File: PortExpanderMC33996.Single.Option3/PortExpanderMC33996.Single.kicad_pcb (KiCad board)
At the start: 2 copper layers, 8 parts, among them J1 DEBUG_CON_01X09, J2 VIKING_CON_01X09, J3 VIKING_CON_01X09, J4 SATA_CON_14P, U1 MC33996EKR2

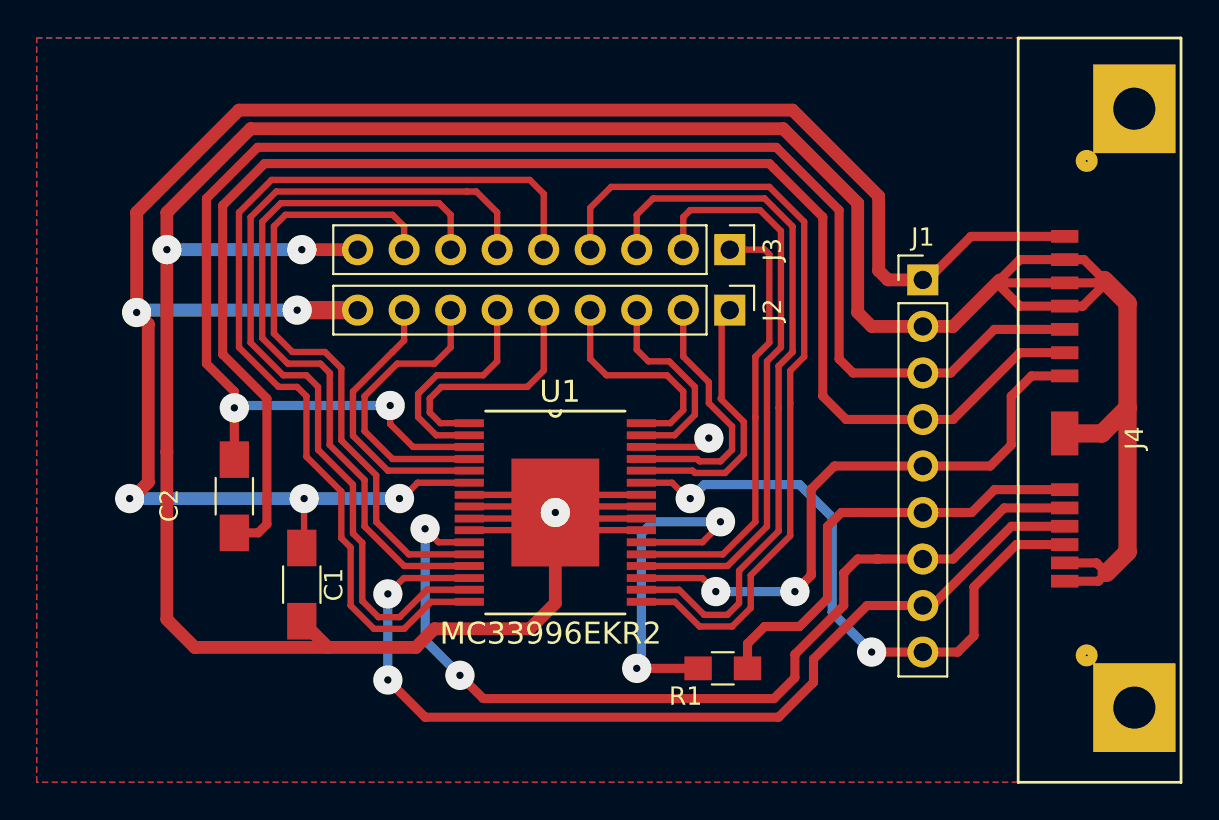
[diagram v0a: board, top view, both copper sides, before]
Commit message: Revision de PCbs + generacion de nuevos archivos Gerber
  - Se corrigen pads de pin headers
  - Se revisan
  - MainBoard option 2
  - PortExpander MC33996.Option3
  - GpibPortExpanderPCA6408A.Option3
  - Se generan Gerber + Vistas 3D
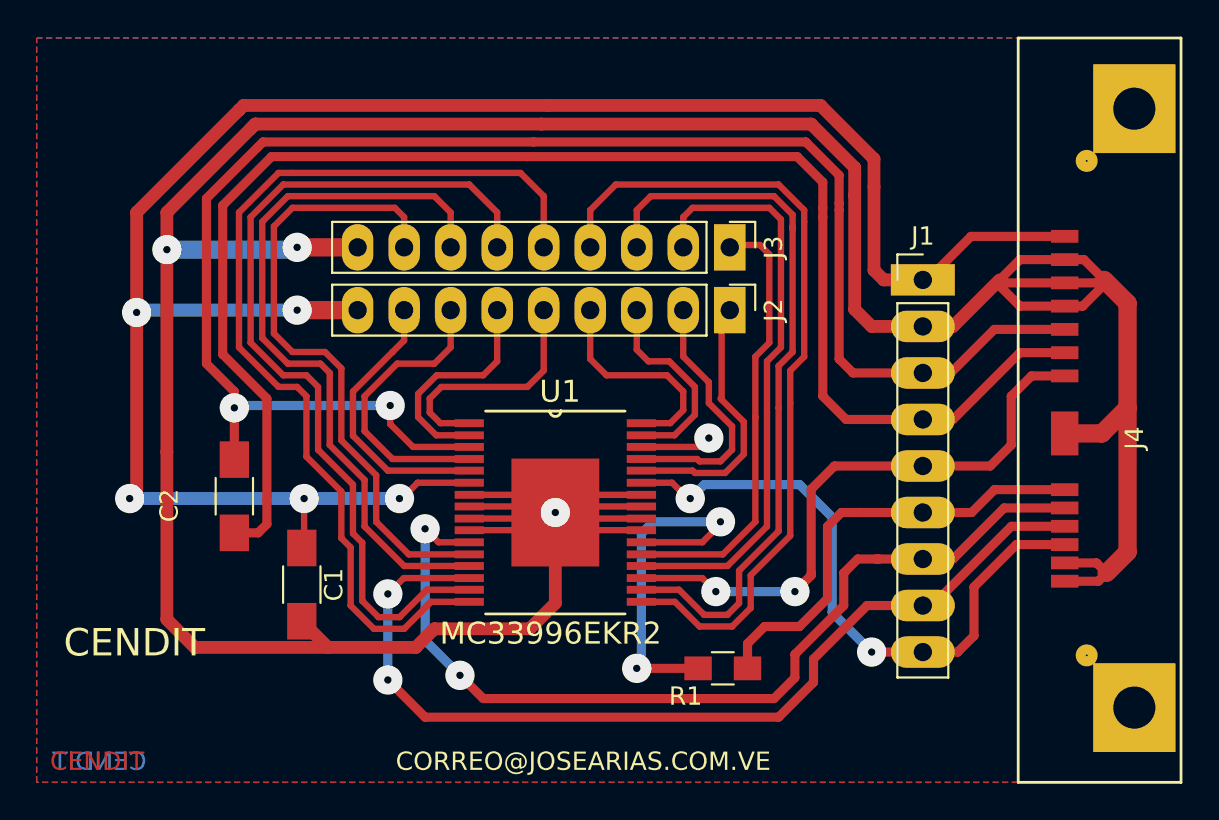
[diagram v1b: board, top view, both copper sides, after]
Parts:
- J1: value DEBUG_CON_01X09 -> DEBUG_CON_9P; footprint Pin_Headers:Pin_Header_Straight_1x09_Pitch2.54mm -> CenditFootprints:DEBUG_CON_9P
- J2, J3: value VIKING_CON_01X09 -> VIKING_CON_9P; footprint Pin_Headers:Pin_Header_Straight_1x09_Pitch2.54mm -> CenditFootprints:VIKING_HEADER_9P
- moved J3 0.13 mm to (146.8, 87.6)
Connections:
- U1 pad 30: (no net) -> /VK_PWM
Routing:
- net /VK_PWM: track 0.00 -> 3.88 mm, vias 0 -> 1
- net (no net): track 3.88 -> 0.00 mm, vias 1 -> 0
- net GNDPWR: track 204.8 -> 206.4 mm
- net GND: track 80.3 -> 81.8 mm
- net VDD: track 88.2 -> 89.5 mm
- net +24.0V: track 110.9 -> 111.8 mm
- net /VKX9: track 39.4 -> 40.0 mm
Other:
- board text added: "CENDIT"
- board text added: "CORREO@JOSEARIAS.COM.VE"

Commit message: Revision de PCBs + generacion nuevos gerber
  - Se hacen ligeras correcciones en los PCBs (5)
  - Se genera nuevamente archivo PCBs combinados
  - Se generan nuevos archivos gerber
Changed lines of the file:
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@@
-(kicad_pcb (version 4) (host pcbnew 4.0.6-e0-6349~53~ubuntu14.04.1)
+(kicad_pcb (version 4) (host pcbnew 4.0.7-e2-6376~58~ubuntu16.04.1)
   (general
     (links 53)
     (no_connects 0)
-    (area 0 0 0 0)
+    (area 106.466 73.7 189.396572 129.192001)
     (thickness 1.6)
     (drawings 10)
-    (tracks 409)
+    (tracks 414)
     (zones 0)
     (modules 8)
@@
   )
   (setup
-    (last_trace_width 0.7)
+    (last_trace_width 0.5)
     (user_trace_width 0.2)
     (user_trace_width 0.35)
@@
   (segment (start 153.631002 84.797002) (end 153.631002 91.020002) (width 0.7) (layer F.Cu) (net 17))
   (segment (start 153.631002 91.020002) (end 154.559 91.948) (width 0.7) (layer F.Cu) (net 17))
-  (segment (start 157.353 91.948) (end 154.559 91.948) (width 0.7) (layer F.Cu) (net 17) (status 400000))
+  (segment (start 157.353 91.948) (end 154.559 91.948) (width 0.7) (layer F.Cu) (net 17))
   (segment (start 136.524004 80.899) (end 120.904 80.899) (width 0.7) (layer F.Cu) (net 17))
   (segment (start 153.631002 83.273002) (end 153.631002 84.797002) (width 0.7) (layer F.Cu) (net 17))
@@
   (segment (start 120.015 80.137) (end 114.427 85.725) (width 0.7) (layer F.Cu) (net 20))
   (segment (start 114.427 91.186) (end 114.427 85.725) (width 0.7) (layer F.Cu) (net 20))
-  (segment (start 155.216004 89.408) (end 157.353 89.408) (width 0.7) (layer F.Cu) (net 20) (status 800000))
+  (segment (start 155.216004 89.408) (end 157.353 89.408) (width 0.7) (layer F.Cu) (net 20))
   (segment (start 154.686 82.804) (end 154.686 84.328) (width 0.7) (layer F.Cu) (net 20))
   (segment (start 151.765 79.883) (end 154.686 82.804) (width 0.7) (layer F.Cu) (net 20))
@@
   (segment (start 129.0066 105.6894) (end 128.143 106.553) (width 0.35) (layer F.Cu) (net 25))
   (segment (start 132.588 105.6894) (end 129.0066 105.6894) (width 0.35) (layer F.Cu) (net 25))
+  (segment (start 144.653 101.346) (end 144.653 101.219) (width 0.5) (layer B.Cu) (net 26))
+  (segment (start 144.653 101.219) (end 145.288 100.584) (width 0.5) (layer B.Cu) (net 26))
+  (segment (start 147.066 100.838) (end 148.082 101.854) (width 0.5) (layer B.Cu) (net 26))
+  (segment (start 148.082 101.854) (end 148.082 103.632) (width 0.5) (layer B.Cu) (net 26))
+  (segment (start 148.082 103.632) (end 149.352 104.902) (width 0.5) (layer B.Cu) (net 26))
+  (segment (start 149.352 104.902) (end 152.908 104.902) (width 0.5) (layer B.Cu) (net 26))
+  (segment (start 152.908 104.902) (end 154.559 106.553) (width 0.5) (layer B.Cu) (net 26))
+  (segment (start 154.559 106.553) (end 154.559 109.728) (width 0.5) (layer B.Cu) (net 26))
+  (via (at 154.559 109.728) (size 1.6) (drill 0.4) (layers F.Cu B.Cu) (net 26))
+  (segment (start 146.812 100.584) (end 147.066 100.838) (width 0.5) (layer B.Cu) (net 26))
+  (segment (start 145.288 100.584) (end 146.812 100.584) (width 0.5) (layer B.Cu) (net 26))
   (segment (start 165.1 103.86) (end 162.459 103.86) (width 0.5) (layer F.Cu) (net 26))
   (segment (start 159.258 109.728) (end 157.353 109.728) (width 0.5) (layer F.Cu) (net 26))
@@
   (segment (start 162.459 103.86) (end 160.147 106.172) (width 0.5) (layer F.Cu) (net 26))
   (segment (start 157.353 109.728) (end 154.559 109.728) (width 0.5) (layer F.Cu) (net 26))
-  (segment (start 152.4 102.362) (end 150.622 100.584) (width 0.5) (layer B.Cu) (net 26))
-  (segment (start 152.4 107.569) (end 152.4 102.362) (width 0.5) (layer B.Cu) (net 26))
-  (segment (start 154.559 109.728) (end 152.4 107.569) (width 0.5) (layer B.Cu) (net 26))
-  (via (at 154.559 109.728) (size 1.6) (drill 0.4) (layers F.Cu B.Cu) (net 26))
   (segment (start 154.051 109.728) (end 154.559 109.728) (width 0.5) (layer F.Cu) (net 26))
-  (segment (start 150.622 100.584) (end 145.415 100.584) (width 0.5) (layer B.Cu) (net 26))
-  (segment (start 145.415 100.584) (end 144.653 101.346) (width 0.5) (layer B.Cu) (net 26))
   (segment (start 144.907 101.092) (end 144.653 101.346) (width 0.5) (layer B.Cu) (net 26))
   (segment (start 143.6624 100.4824) (end 141.986 100.4824) (width 0.35) (layer F.Cu) (net 26))
